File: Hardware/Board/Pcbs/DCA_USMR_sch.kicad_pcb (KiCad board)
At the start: 4 copper layers, 66 x 68.6 mm, 56 parts, among them J1 Conn_02x03_Counter_Clockwise, J3 Barrel_Jack_Switch, U1 ATSAMD, U2 LD1117S33TR_SOT223, U3 ATWINC1500-MR, U4 ENC28J60, Y1 25MHz

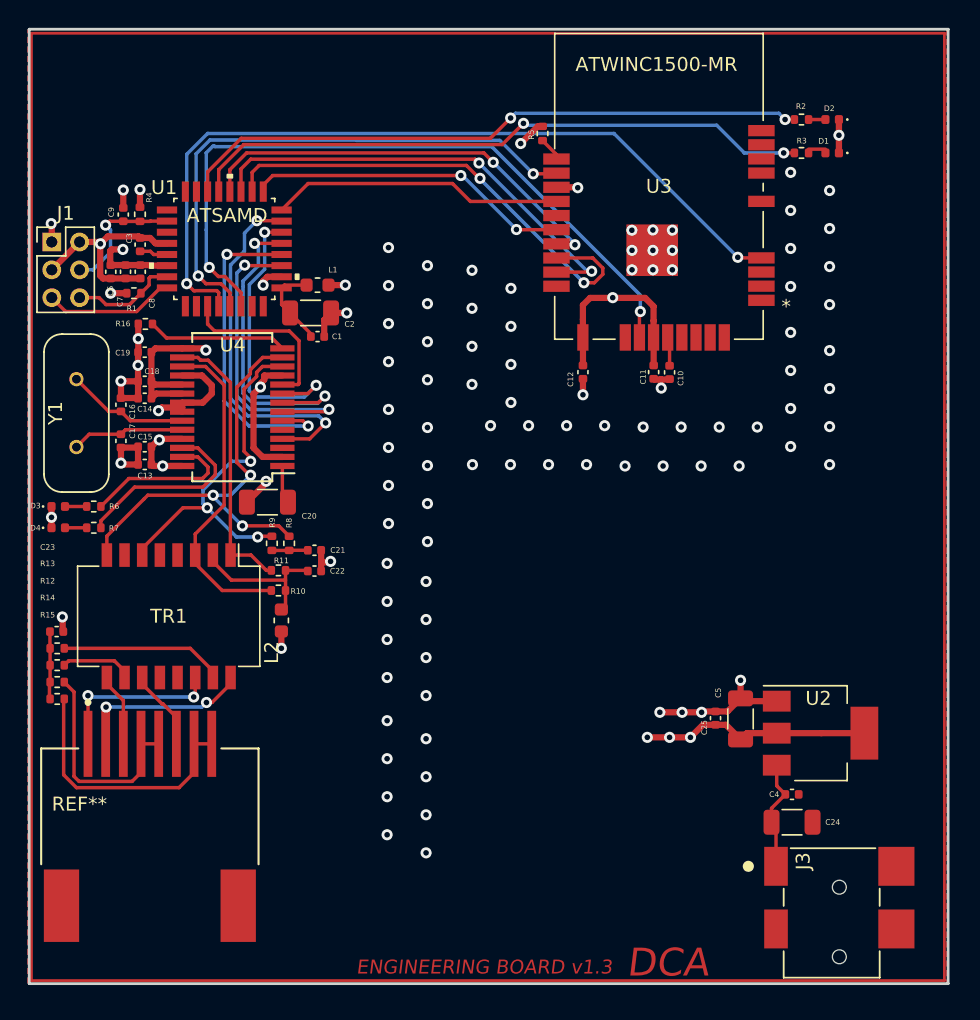
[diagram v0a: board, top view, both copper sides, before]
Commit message: Newest board spin. Fixed Wifi, and ethernet SPI ports. Added Sensor connectors with digital In/Outs
Signed-off-by: Darren <Darmor>
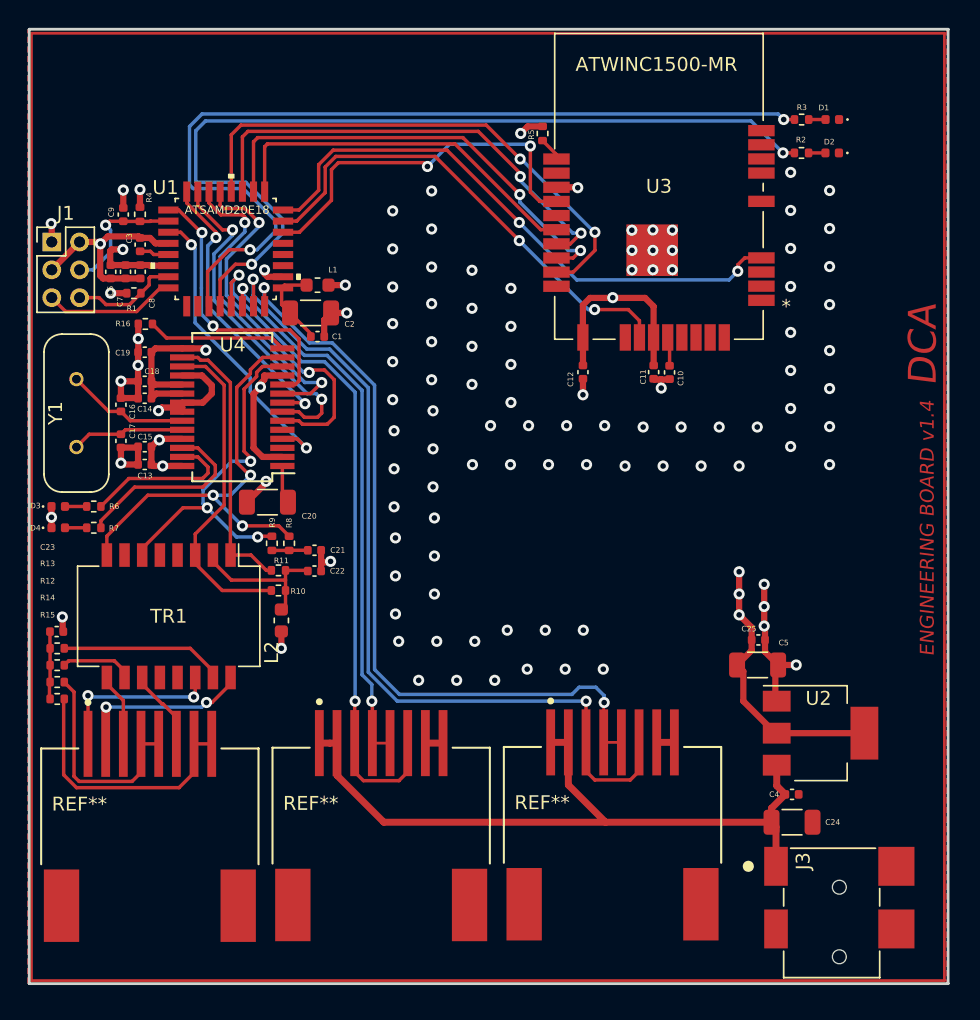
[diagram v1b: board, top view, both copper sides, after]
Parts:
- added REF**: , eec:Amphenol_ICC-RJLSE4208101T-MFG, F.Cu at (226.3, 152.5)
- added REF**: , eec:Amphenol_ICC-RJLSE4208101T-MFG, F.Cu at (242.9, 152.4)
- U1: value ATSAMD -> ATSAMD20E18
- moved C25 6.41 mm to (253.4, 136.1), turned to 0 degrees
- moved C5 4.06 mm to (253.3, 137.9), turned to 0 degrees
- moved D1 2.40 mm to (258.7, 98.7)
- moved R3 2.40 mm to (256.5, 98.7)
- moved D2 2.40 mm to (258.7, 101.1)
- moved R2 2.40 mm to (256.5, 101.1)
- moved U1 0.10 mm to (215.1, 108.0)
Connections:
- R2 pad 2: Net-(R2-Pad2) -> Net-(U1-Pad4)
- R3 pad 2: Net-(R3-Pad2) -> Net-(U1-Pad3)
- U1 pad 11: ENC_MOSI -> unconnected-(U1-Pad11)
- U1 pad 12: ENC_MISO -> unconnected-(U1-Pad12)
- U1 pad 13: ENC_SCK -> unconnected-(U1-Pad13)
- U1 pad 14: ENC_SS -> WINC_EXTINT
- U1 pad 15: ENC_EXTINT -> WINC_CHIP_EN
- U1 pad 16: WINC_EXTINT -> WINC_RESET
- U1 pad 19: WINC_SCK -> WINC_SS
- U1 pad 20: WINC_SS -> WINC_SCK
- U1 pad 21: Net-(R3-Pad2) -> ENC_MISO
- U1 pad 22: Net-(R2-Pad2) -> ENC_SS
- U1 pad 23: unconnected-(U1-Pad23) -> ENC_MOSI
- U1 pad 24: unconnected-(U1-Pad24) -> ENC_SCK
- U1 pad 25: unconnected-(U1-Pad25) -> ENC_RESET
- U1 pad 27: unconnected-(U1-Pad27) -> ENC_EXTINT
- U1 pad 3: ENC_RESET -> Net-(U1-Pad3)
- U1 pad 4: WINC_RESET -> Net-(U1-Pad4)
- U1 pad 5: WINC_WAKE -> SENSOR1_IN
- U1 pad 6: WINC_CHIP_EN -> SENSOR1_OUT
- U1 pad 7: unconnected-(U1-Pad7) -> SENSOR2_IN
- U1 pad 8: unconnected-(U1-Pad8) -> SENSOR2_OUT
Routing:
- net Net-(U1-Pad3): track 0.00 -> 64.8 mm, vias 0 -> 2
- net Net-(U1-Pad4): track 0.00 -> 64.1 mm, vias 0 -> 2
- net SENSOR2_IN: track 0.00 -> 62.5 mm, vias 0 -> 2
- net SENSOR2_OUT: track 0.00 -> 55.4 mm, vias 0 -> 2
- net SENSOR1_IN: track 0.00 -> 49.4 mm, vias 0 -> 2
- net Net-(R2-Pad2): track 45.5 -> 0.00 mm, vias 2 -> 0
- net Net-(R3-Pad2): track 45.2 -> 0.00 mm, vias 2 -> 0
- net Net-(C24-Pad1): track 8.07 -> 52.4 mm
- net SENSOR1_OUT: track 0.00 -> 40.0 mm, vias 0 -> 2
- net WINC_WAKE: track 39.9 -> 0.00 mm, vias 2 -> 0
- net WINC_CHIP_EN: track 51.2 -> 34.7 mm
- net WINC_RESET: track 58.5 -> 42.0 mm
- net ENC_RESET: track 12.7 -> 21.2 mm, vias 0 -> 2
- net WINC_EXTINT: track 21.1 -> 27.4 mm, vias 0 -> 2
- net WINC_SCK: track 33.0 -> 38.4 mm
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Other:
- board text added: "ENGINEERING BOARD v1.4"
- board text removed: "ENGINEERING BOARD v1.3"
